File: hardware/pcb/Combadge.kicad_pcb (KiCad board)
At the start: 2 copper layers, 27 parts, among them J1 Conn_01x05_Female, J2 USB_B_Micro, J3 TOUCH, U1 XC6808A4D28R-G, U2 ESP32-WROOM-32, U3 NCP160AMX330TBG, U4 NAU8315YG

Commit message: Add basic PCB outline
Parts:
- C2, C6, C7: value 100pF -> 0.1uF
- U4: moved to B.Cu
- moved BT1 58.2 mm to (86.4, 52.8), turned to 180 degrees
- moved J2 56.6 mm to (94.6, 61.2), turned to 90 degrees
- moved C2 45.9 mm to (66.5, 72.6)
- moved U4 44.8 mm to (78.0, 64.8), turned to 180 degrees
- moved J3 44.2 mm to (85.6, 72.4)
- moved C1 41.7 mm to (72.1, 72.6), turned to 180 degrees
- moved R5 35.9 mm to (52.5, 90.5)
- moved J1 35.8 mm to (70.6, 48.0), turned to 90 degrees
- moved MK1 28.4 mm to (87.9, 59.9)
- moved U1 22.4 mm to (138.0, 70.0)
- moved U2 21.3 mm to (73.2, 61.0), turned to 90 degrees
- moved LS1 19.6 mm to (86.1, 67.8), turned to 180 degrees
- moved C3 4.14 mm to (109.9, 59.0)
- moved MOSFET1 3.97 mm to (151.9, 78.8)
- moved C5 2.96 mm to (76.0, 86.0)
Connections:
- net -BATT renamed GND
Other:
- board outline added: 45 x 32.3 mm

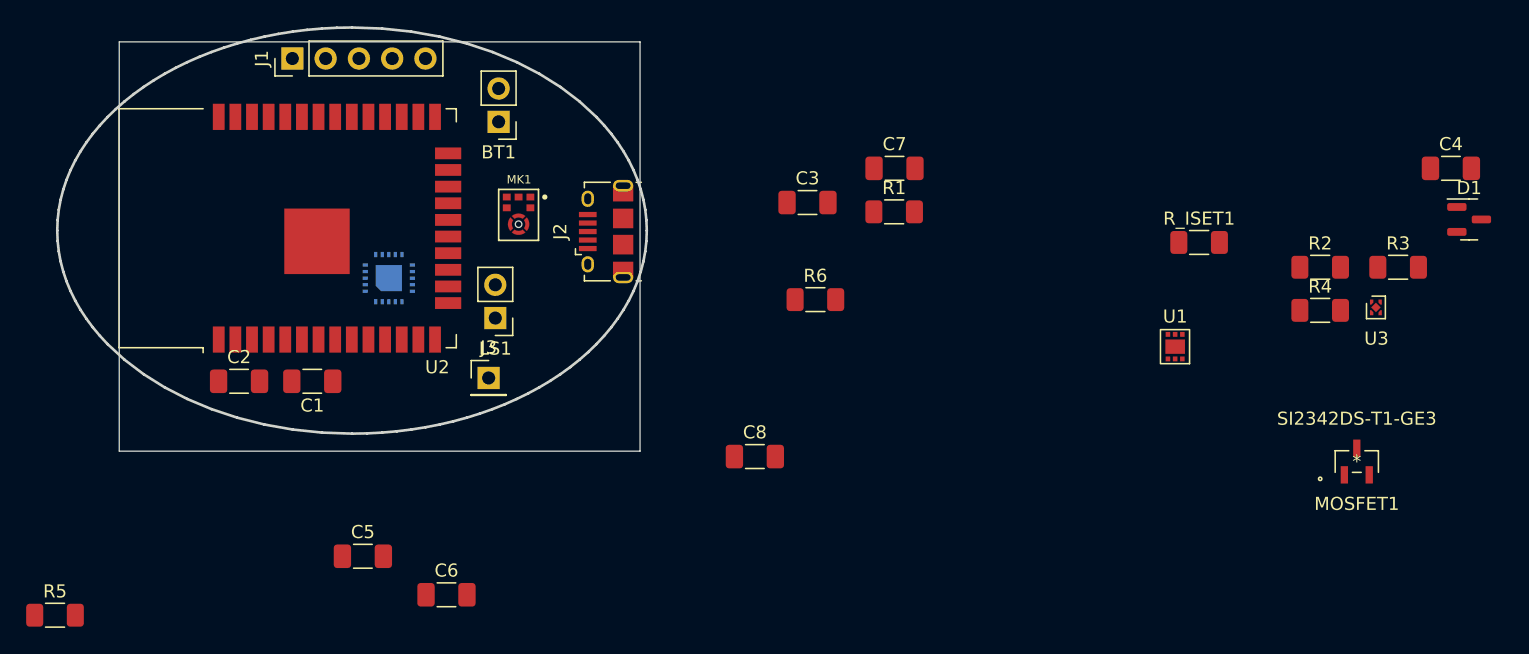
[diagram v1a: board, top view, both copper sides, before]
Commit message: Route microphone
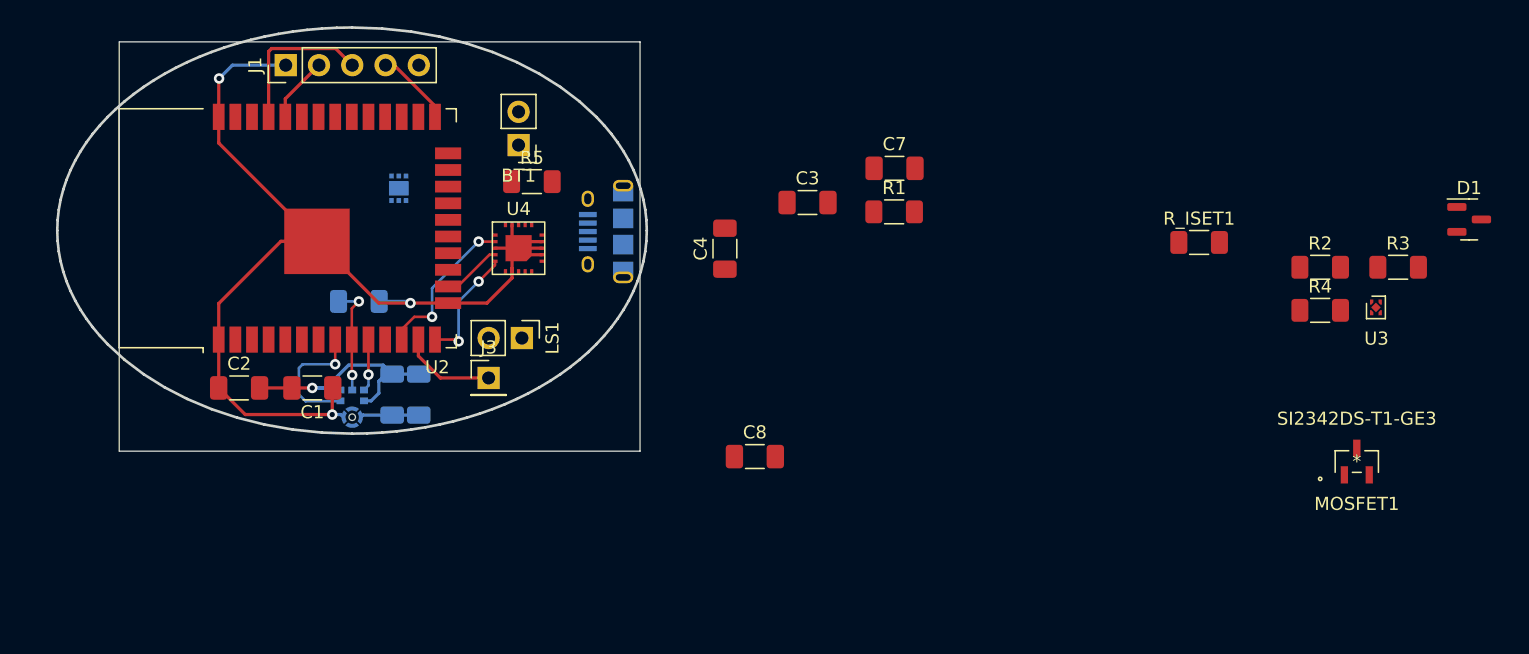
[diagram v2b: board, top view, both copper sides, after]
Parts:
- C5, C6, J2, MK1, R6, U1: moved to B.Cu
- U4: moved to F.Cu
- moved U1 60.5 mm to (78.7, 57.9), turned to 180 degrees
- moved C4 55.8 mm to (103.6, 62.5), turned to 90 degrees
- moved R5 49.2 mm to (88.9, 57.4)
- moved R6 34.8 mm to (75.7, 66.5)
- moved MK1 19.5 mm to (75.2, 74.7), turned to 180 degrees
- moved C6 15.8 mm to (78.2, 73.7), turned to 90 degrees
- moved C5 13.1 mm to (80.3, 73.7), turned to 90 degrees
- moved U4 10.2 mm to (87.9, 62.5), turned to 0 degrees
- moved LS1 2.54 mm to (88.1, 69.3), turned to -90 degrees
- moved BT1 2.34 mm to (87.9, 54.6)
- moved J1 0.72 mm to (70.1, 48.5)
- moved C1 0.51 mm to (72.1, 73.2)
- moved C2 0.51 mm to (66.6, 73.2)
- turned J2 to -90 degrees
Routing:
- net GND: track 0.00 -> 86.4 mm, vias 0 -> 3
- net +3.3V: track 0.00 -> 18.9 mm, vias 0 -> 1
- net /ESP_TX: track 0.00 -> 12.0 mm
- net /SPK_SD: track 0.00 -> 12.0 mm, vias 0 -> 2
- net /MIC_BCLK: track 0.00 -> 10.2 mm, vias 0 -> 1
- net /SPK_BCLK: track 0.00 -> 9.12 mm, vias 0 -> 2
- net /MIC_SD: track 0.00 -> 8.55 mm, vias 0 -> 2
- net Net-(J3-Pad1): track 0.00 -> 7.31 mm
- net /ESP_BOOT: track 0.00 -> 5.90 mm
- net /ESP_RX: track 0.00 -> 5.01 mm
- net /SPK_WS: track 0.00 -> 4.58 mm
- net /MIC_WS: track 0.00 -> 3.99 mm, vias 0 -> 1

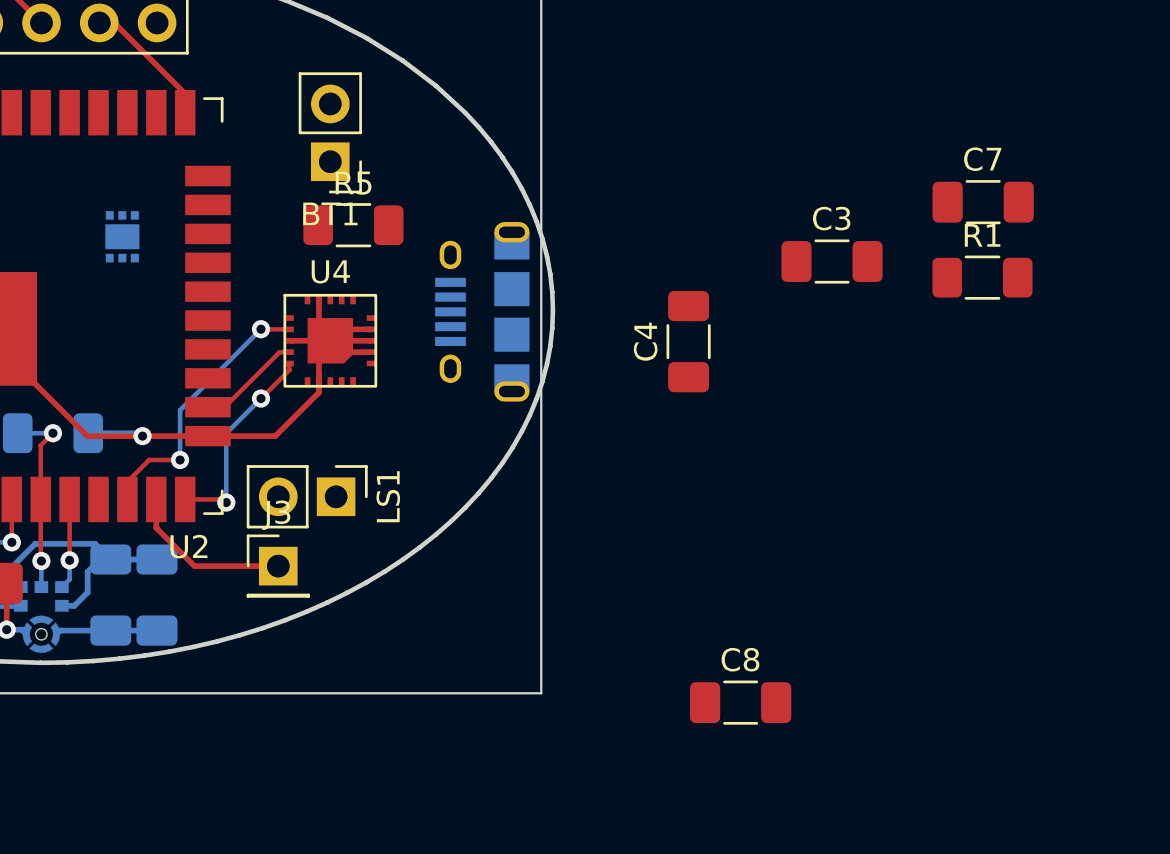
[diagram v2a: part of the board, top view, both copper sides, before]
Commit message: Move incorrectly placed capacitors around microphone
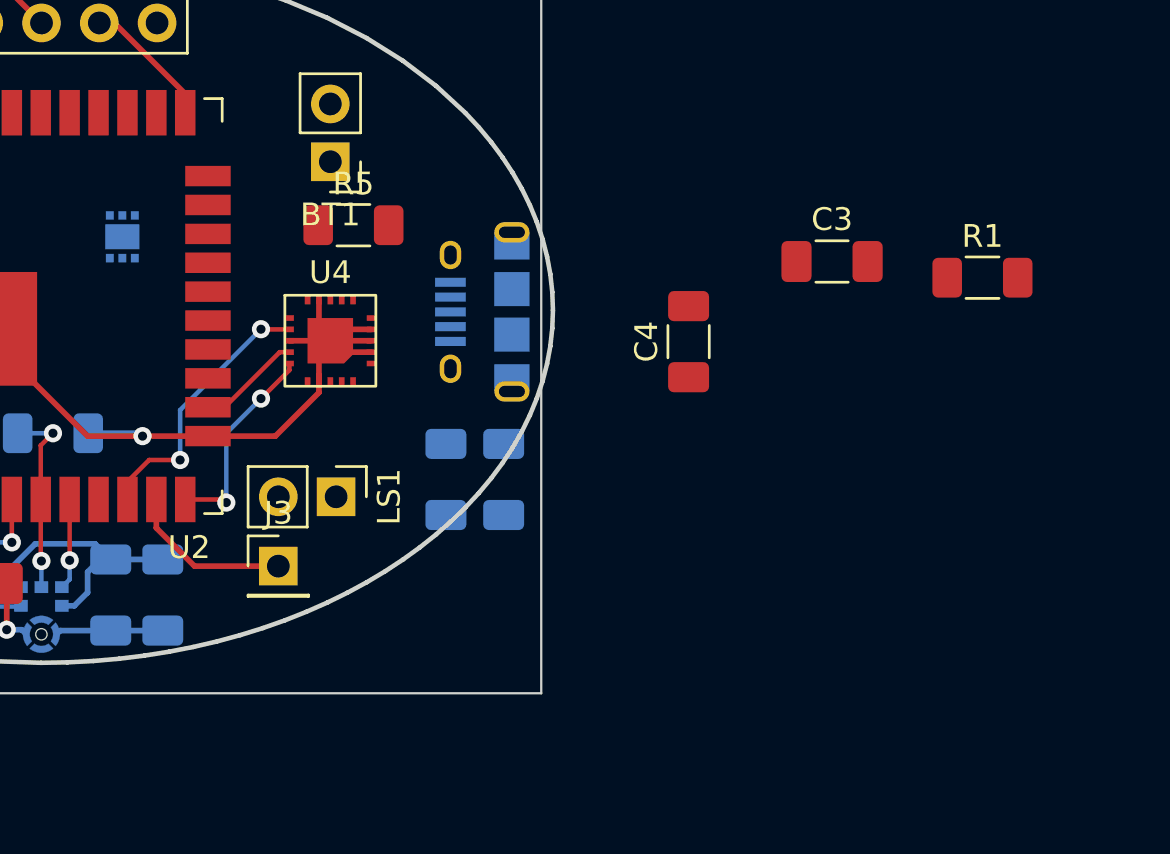
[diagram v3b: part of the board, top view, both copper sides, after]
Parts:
- C7, C8: moved to B.Cu
- moved C7 42.1 mm to (78.2, 73.7), turned to 90 degrees
- moved C8 25.8 mm to (80.5, 73.7), turned to 90 degrees
- moved C6 18.0 mm to (95.5, 68.6)
- moved C5 13.7 mm to (93.0, 68.6)

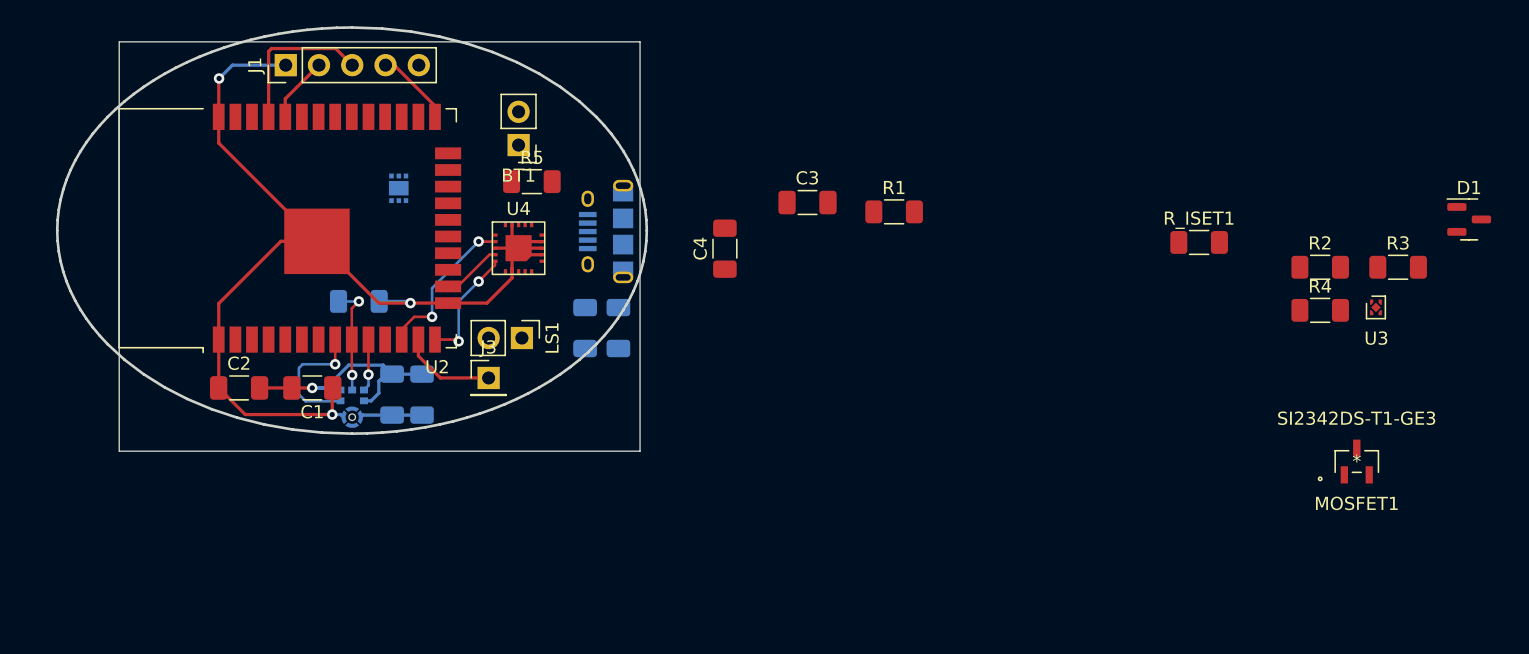
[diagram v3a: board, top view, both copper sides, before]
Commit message: Route speaker and amplifier
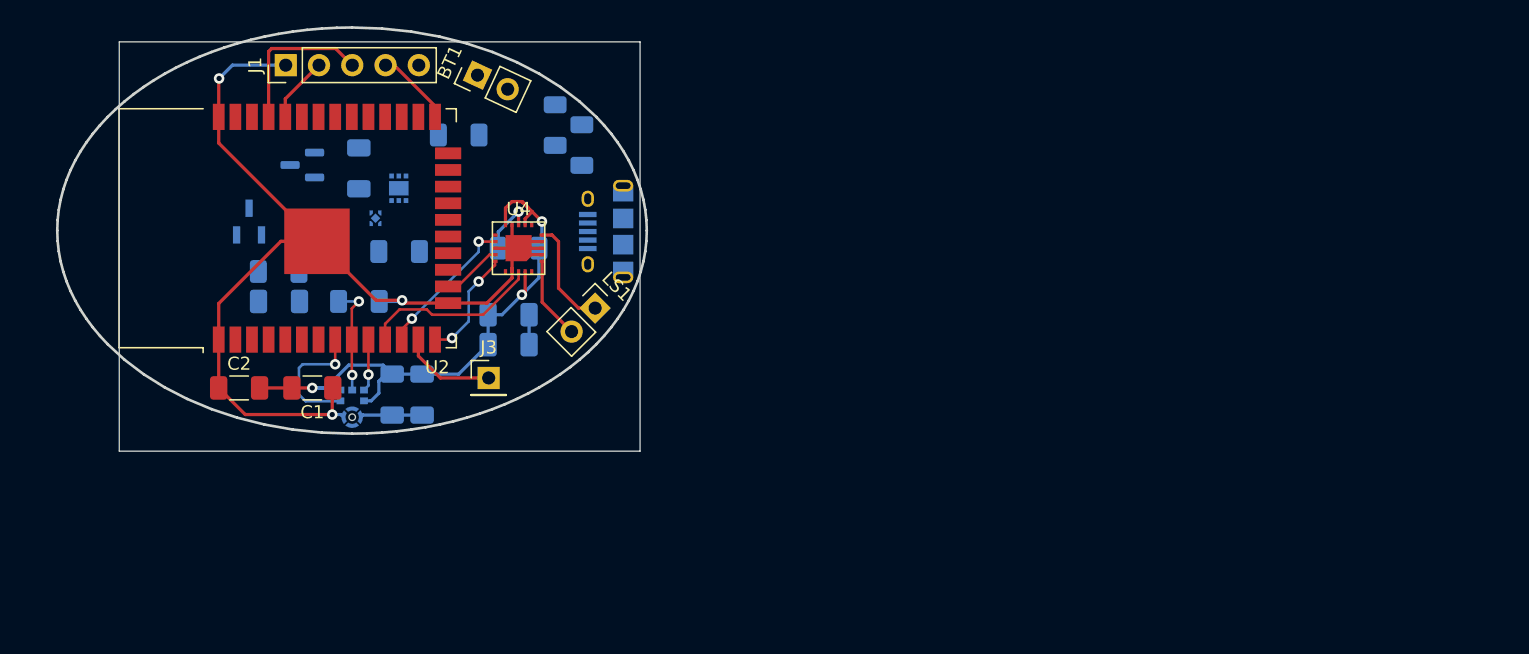
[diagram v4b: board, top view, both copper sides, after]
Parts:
- C3, C4, D1, MOSFET1, R1, R2, R3, R4, R5, R_ISET1, U3: moved to B.Cu
- moved D1 89.2 mm to (71.4, 56.1), turned to 180 degrees
- moved MOSFET1 86.5 mm to (67.3, 60.5), turned to 180 degrees
- moved U3 76.7 mm to (77.0, 60.2), turned to 180 degrees
- moved R4 70.4 mm to (78.8, 62.7), turned to 180 degrees
- moved R3 63.0 mm to (92.7, 54.6), turned to -90 degrees
- moved R2 59.4 mm to (90.7, 53.1), turned to -90 degrees
- moved R_ISET1 57.1 mm to (83.3, 53.8), turned to 180 degrees
- moved R1 47.2 mm to (69.6, 64.3), turned to 180 degrees
- moved C3 41.0 mm to (69.6, 66.5), turned to 180 degrees
- moved C4 28.6 mm to (75.7, 56.4)
- moved C6 8.44 mm to (87.1, 67.6), turned to 180 degrees
- moved BT1 6.19 mm to (84.7, 49.3), turned to 65 degrees
- moved LS1 6.04 mm to (93.7, 67.1), turned to -45 degrees
- moved C5 5.98 mm to (87.1, 69.8), turned to 180 degrees
- moved R5 5.18 mm to (87.9, 62.5)
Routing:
- net +3.3V: track 18.9 -> 45.4 mm, vias 1 -> 3
- net /SPK_EN: track 0.00 -> 13.7 mm
- net Net-(LS1-Pad1): track 0.00 -> 8.45 mm
- net Net-(LS1-Pad2): track 0.00 -> 6.30 mm
- net Net-(R5-Pad1): track 0.00 -> 4.43 mm, vias 0 -> 1
- net GND: track 86.4 -> 88.1 mm
- net /SPK_SD: track 12.0 -> 11.2 mm
- net /SPK_BCLK: track 9.12 -> 8.56 mm

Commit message: Finish initial version of PCB
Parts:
- D1: value 3V -> D_Zener_Dual_CommonAnode_KKA
- R1: moved to F.Cu
- moved R1 8.91 mm to (70.1, 73.2), turned to 90 degrees
- moved D1 7.64 mm to (74.2, 63.2)
- moved R3 4.95 mm to (87.9, 55.9), turned to 90 degrees
- moved R_ISET1 3.84 mm to (82.8, 57.7), turned to -90 degrees
- moved C3 3.31 mm to (66.3, 66.3), turned to 0 degrees
- moved C4 3.31 mm to (73.9, 59.2), turned to 180 degrees
- moved MOSFET1 3.31 mm to (70.1, 62.2)
- moved R2 2.83 mm to (90.2, 55.9), turned to 90 degrees
- moved U3 2.65 mm to (79.5, 61.0), turned to -90 degrees
- moved U1 0.80 mm to (79.5, 58.2), turned to -90 degrees
- moved R4 0.58 mm to (78.5, 63.2)
- moved C1 0.25 mm to (72.4, 73.2), turned to 90 degrees
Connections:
- D1 pad 2: Net-(D1-Pad2) -> unconnected-(D1-Pad2)
- D1 pad 3: (no net) -> Net-(MOSFET1-Pad1)
- MOSFET1 pad 1: Net-(D1-Pad2) -> Net-(MOSFET1-Pad1)
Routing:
- net GND: track 88.1 -> 131.4 mm, vias 3 -> 6
- net +3.3V: track 45.4 -> 81.6 mm
- net +BATT: track 0.00 -> 21.5 mm
- net Net-(J2-Pad1): track 0.00 -> 14.2 mm
- net Net-(C4-Pad2): track 0.00 -> 11.0 mm
- net Net-(J2-Pad2): track 0.00 -> 10.1 mm
- net Net-(J2-Pad3): track 0.00 -> 8.88 mm
- net Net-(C3-Pad2): track 0.00 -> 7.49 mm, vias 0 -> 1
- net /Power/CHRG_STATUS: track 0.00 -> 6.53 mm, vias 0 -> 1
- net Net-(R4-Pad2): track 0.00 -> 2.22 mm
- net Net-(MOSFET1-Pad1): track 0.00 -> 2.18 mm
- net Net-(R_ISET1-Pad2): track 0.00 -> 1.87 mm
- net /ESP_BOOT: track 5.90 -> 4.41 mm
- net /SPK_WS: track 4.58 -> 3.85 mm
- added copper zone on B.Cu, net GND
- added copper zone on F.Cu, net GND
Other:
- board size 45 x 32.3 mm -> 45 x 31 mm
